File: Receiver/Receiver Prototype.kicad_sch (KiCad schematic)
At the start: 70 parts, among them J1 Conn_01x02_Socket, J10 Conn_01x01, J11 Conn_Coaxial, J12 Conn_Coaxial, J2 Conn_01x03, J3 Conn_01x01, J4 Conn_Coaxial, J5 Conn_01x01, J6 Conn_01x02, J7 Conn_Coaxial, J8 Conn_Coaxial, J9 Conn_01x01, U1 OPA3692ID, U2 AD8692ARZ, U3 OPA692IDBVR, U5 AD607ARSZ

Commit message: Receiver schematic complete. ERC not passed due to issues with GND
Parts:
- removed J2: Conn_01x03, Connector_PinHeader_2.54mm:PinHeader_1x03_P2.54mm_Vertical, symbol Connector_Generic:Conn_01x03
- removed JP1: Jumper_2_Bridged, symbol Jumper:Jumper_2_Bridged
- added C27, C33: 4.7u, Capacitor_SMD:C_0603_1608Metric_Pad1.08x0.95mm_HandSolder, symbol Device:C
- added C28, C35: 10u, Capacitor_SMD:C_0603_1608Metric_Pad1.08x0.95mm_HandSolder, symbol Device:C
- added C29, C31, C34: 0.47u, Capacitor_SMD:C_0603_1608Metric_Pad1.08x0.95mm_HandSolder, symbol Device:C
- added C30, C32, C36, C37: C, Capacitor_SMD:C_0603_1608Metric_Pad1.08x0.95mm_HandSolder, symbol Device:C
- added J13, J14: Conn_Coaxial, BNC 112404:CONN_112404_AMP, symbol Connector:Conn_Coaxial
- added J15, J16, J17, J18, J19, J2, J21, J22: Conn_01x01, Connector_PinHeader_2.54mm:PinHeader_1x01_P2.54mm_Vertical, symbol Connector_Generic:Conn_01x01
- added J23, J24: Conn_01x02, Connector_PinHeader_2.54mm:PinHeader_1x02_P2.54mm_Vertical, symbol Connector_Generic:Conn_01x02
- added R20, R22: 49.9k, Resistor_SMD:R_0603_1608Metric_Pad0.98x0.95mm_HandSolder, symbol Device:R
- added R21: 33.2k, Resistor_SMD:R_0603_1608Metric_Pad0.98x0.95mm_HandSolder, symbol Device:R
- added U4, U7: LT3045EMSE-PBF, LT3045 MSOP:MSOP12_MSE_ADI, symbol LT3045 MSOP:LT3045EMSE-PBF
- added U6: LT3094EMSE-PBF, LT3094 MSOP:05-08-1666_ADI, symbol LT3094 MSOP:LT3094EMSE-PBF
- J10, J3, J9: footprint Connector_PinSocket_2.54mm:PinSocket_1x01_P2.54mm_Vertical -> Connector_PinHeader_2.54mm:PinHeader_1x01_P2.54mm_Vertical
- J11, J12, J4, J7, J8: footprint BNC 112404:CONN_112404_AMP -> Connector_Coaxial:SMA_Amphenol_132289_EdgeMount
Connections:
- net GND: now also C27.2, C28.2, C29.2, C30.2, C31.2, C32.2, C33.2, C34.2, C35.2, J13.2 (Ext), J14.2 (Ext), R20.2, R21.2, R22.2, U4.6 (ILIM), U4.9 (GND), U4.EPAD (GND), U6.6 (ILIM), U6.9 (GND), U7.6 (ILIM), U7.9 (GND), U7.EPAD (GND)
- net IC_Gain: now also J21.1 (Pin_1)
- net IC_I: now also J23.1 (Pin_1)
- net IC_IFOP: now also J22.1 (Pin_1)
- net IC_Q: now also J23.2 (Pin_2)
- net INA: now also C36.1, C37.1
- net INB: now also C36.2, C37.2
- net Reference_In: now also J16.1 (Pin_1)
- net Reference_Out: now also J17.1 (Pin_1)
- net VCC: now also C28.1, J18.1 (Pin_1), U4.10 (OUTS), U4.11 (OUT)
- net VEE: now also C32.1, J19.1 (Pin_1), U6.10 (OUTS), U6.11 (OUT)
- net at U5.7 (GREF): now also C17.2, R16.1, U5.9 (VMID)
- net +3V renamed +3.3_out
- net +3.3_out: now also J24.2 (Pin_2)
- new net: C34.1, R21.1, U7.8 (SET)
- new net: C29.1, R22.1, U4.8 (SET)
- new net: C31.1, R20.1, U6.8 (SET)
- new net +3.3V: C35.1, J24.1 (Pin_1), U7.10 (OUTS), U7.11 (OUT)
- new net PWR+: C27.1, C33.1, J13.1 (In), J2.1 (Pin_1), U4.1 (IN), U4.4 (EN/UV), U4.7 (PGFB), U7.1 (IN), U7.4 (EN/UV), U7.7 (PGFB)
- new net PWR-: C30.1, J14.1 (In), J15.1 (Pin_1), U6.2 (IN), U6.3 (EN/UV), U6.5 (PGFB)
- no-connect marks 11 -> 24
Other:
- note added: "+3.3V circut"
- note added: "VEE circut"
- moved on the sheet: C1, C16, C17, C18, C19, C2, C20, C21, C22, C23, C24, C25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

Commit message: Receiver ready for DR2. DRC not passed due to SMA connectors
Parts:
- removed C33: 4.7u, Capacitor_SMD:C_0603_1608Metric_Pad1.08x0.95mm_HandSolder, symbol Device:C
- removed C34: 0.47u, Capacitor_SMD:C_0603_1608Metric_Pad1.08x0.95mm_HandSolder, symbol Device:C
- removed C35: 10u, Capacitor_SMD:C_0603_1608Metric_Pad1.08x0.95mm_HandSolder, symbol Device:C
- removed J16, J17, J18, J19: Conn_01x01, Connector_PinHeader_2.54mm:PinHeader_1x01_P2.54mm_Vertical, symbol Connector_Generic:Conn_01x01
- removed U7: LT3045EMSE-PBF, LT3045 MSOP:MSOP12_MSE_ADI, symbol LT3045 MSOP:LT3045EMSE-PBF
- added J17, J18, J28: Conn_01x02, Connector_PinHeader_2.54mm:PinHeader_1x02_P2.54mm_Vertical, symbol Connector_Generic:Conn_01x02
- added J20, J25: Conn_01x01, Connector_PinHeader_2.54mm:PinHeader_1x01_P2.54mm_Vertical, symbol Connector_Generic:Conn_01x01
- added J26, J27: Conn_01x03, Connector_PinHeader_2.54mm:PinHeader_1x03_P2.54mm_Vertical, symbol Connector_Generic:Conn_01x03
- C30, C32: value C -> 10u
- C31: value 0.47u -> 4.7u
- J5: footprint Connector_PinSocket_2.54mm:PinSocket_1x01_P2.54mm_Vertical -> Connector_PinHeader_2.54mm:PinHeader_1x01_P2.54mm_Vertical
- R10, R13, R14: value R -> 100
- R21: value 33.2k -> 1k
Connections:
- net +3.3V is gone; now on net VCC: J24.1 (Pin_1)
- net GND: now also D3.2 (A), D4.1 (K), R14.1, J20.1 (Pin_1), J25.1 (Pin_1); no longer R21.2
- net INA: now also J28.1 (Pin_1)
- net INB: now also J28.2 (Pin_2)
- net Inst_Out: now also J18.1 (Pin_1), J18.2 (Pin_2)
- net PWR+: now also J26.1 (Pin_1)
- net PWR-: now also U6.13 (IN), J27.1 (Pin_1); no longer U6.2 (IN)
- net Reference_Out: now also J17.1 (Pin_1), J17.2 (Pin_2)
- net VCC: now also J26.2 (Pin_2); no longer C28.1, U4.10 (OUTS), U4.11 (OUT)
- net VEE: now also J27.2 (Pin_2); no longer C32.1, U6.10 (OUTS), U6.11 (OUT)
- net at R21.1: now also U5.19 (FLTR)
- net at C22.1: now also R21.2; no longer U5.19 (FLTR)
- net +3.3_out renamed VCC_IC
- new net VCC_In: C28.1, J26.3 (Pin_3), U4.10 (OUTS), U4.11 (OUT)
- new net VEE_In: C32.1, J27.3 (Pin_3), U6.10 (OUTS), U6.11 (OUT)
- no-connect marks 24 -> 20
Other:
- note removed: "+3.3V circut"
- moved on the sheet: C19, C21, C22, C30, C31, C32, J13, J14, J15, J2, R20, U6

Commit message: DR2
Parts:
- J13, J14: footprint BNC 112404:CONN_112404_AMP -> Connector_Coaxial:BNC_Amphenol_B6252HB-NPP3G-50_Horizontal
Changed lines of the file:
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@@
 	(wire
 		(pts
-			(xy 179.07 285.75) (xy 179.07 283.21)
-		)
-		(stroke
-			(width 0)
-			(type default)
-		)
-	)
-	(wire
-		(pts
 			(xy 262.89 179.07) (xy 262.89 172.72)
 		)
@@
 			)
 		)
-		(property "Footprint" "BNC 112404:CONN_112404_AMP"
+		(property "Footprint" "Connector_Coaxial:BNC_Amphenol_B6252HB-NPP3G-50_Horizontal"
 			(at 114.3 25.4 0)
 			(effects
@@
 			)
 		)
-		(property "Footprint" "BNC 112404:CONN_112404_AMP"
+		(property "Footprint" "Connector_Coaxial:BNC_Amphenol_B6252HB-NPP3G-50_Horizontal"
 			(at 66.04 25.4 0)
 			(effects

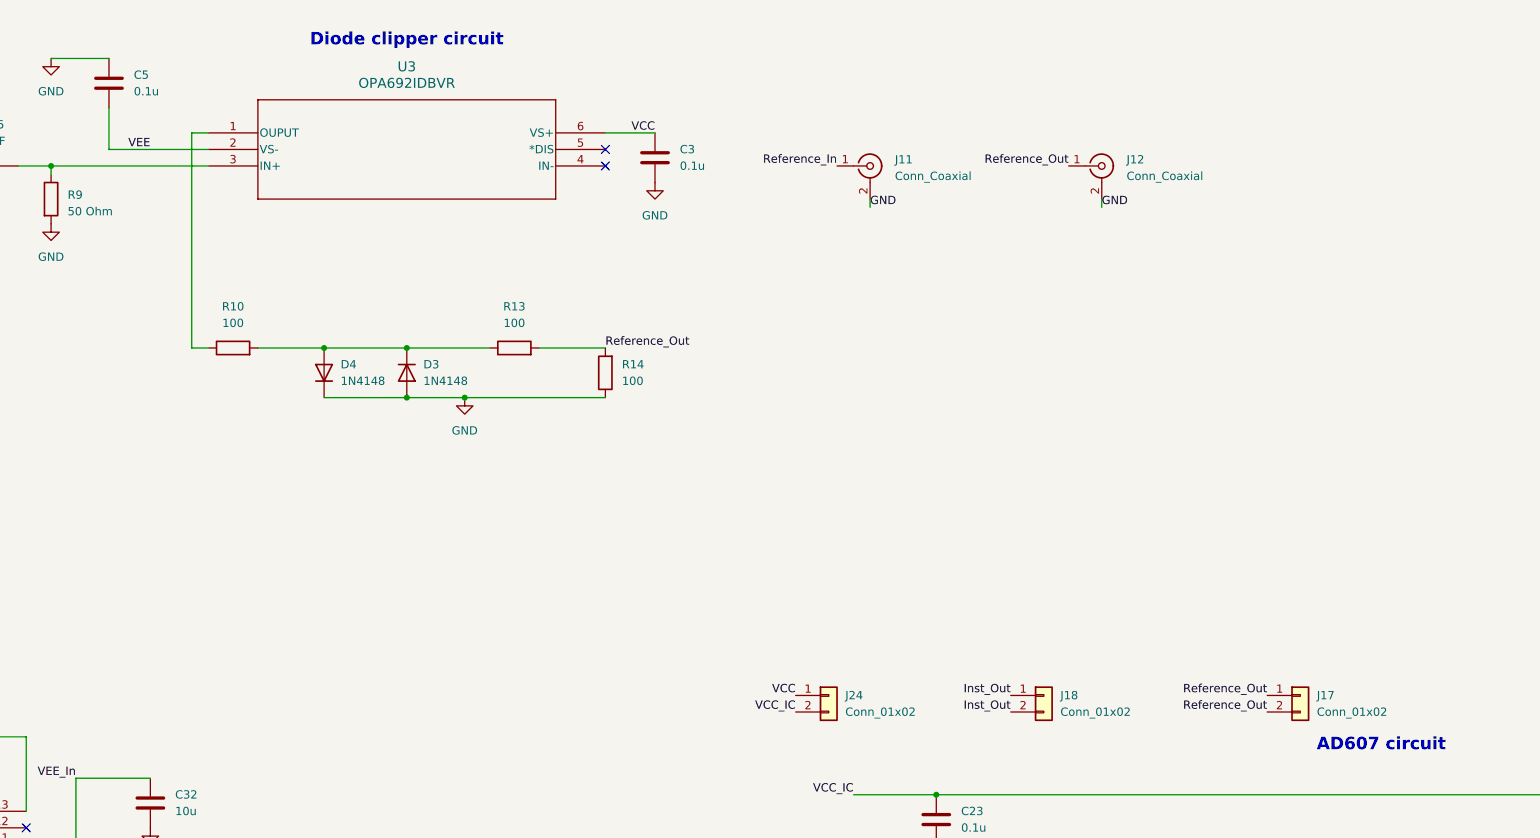
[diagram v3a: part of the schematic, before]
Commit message: Moved some components. Design not complete for the DR2
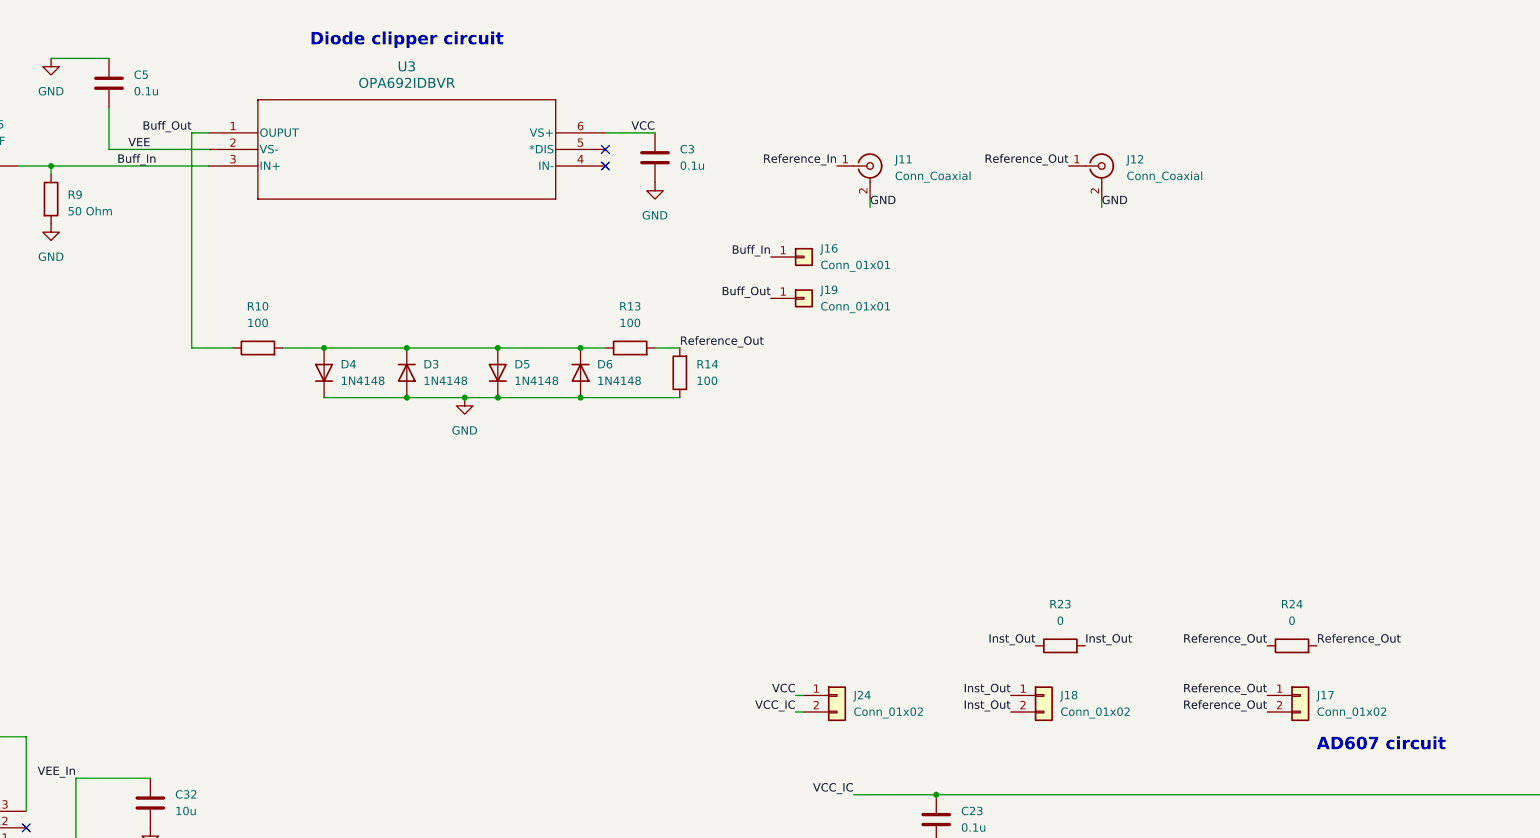
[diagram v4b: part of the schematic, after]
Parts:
- added D5, D6: 1N4148, Diode_SMD:D_0805_2012Metric_Pad1.15x1.40mm_HandSolder, symbol Diode:1N4148
- added J16, J19: Conn_01x01, Connector_PinHeader_2.54mm:PinHeader_1x01_P2.54mm_Vertical, symbol Connector_Generic:Conn_01x01
- added R23, R24: 0, Resistor_SMD:R_0603_1608Metric_Pad0.98x0.95mm_HandSolder, symbol Device:R
- J1: footprint Connector_PinSocket_2.54mm:PinSocket_1x02_P2.54mm_Vertical -> Connector_PinSocket_2.54mm:PinSocket_1x02_P2.54mm_Horizontal
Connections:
- net GND: now also D5.1 (K), D6.2 (A)
- net Inst_Out: now also R23.1, R23.2
- net Reference_Out: now also R24.1, R24.2
- net at D3.1 (K), D4.2 (A), R10.2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: now also D5.2 (A), D6.1 (K)
- net Buff_Out: now reaches R10.1, U3.1 (OUPUT)
- net Buff_Out: now also J19.1 (Pin_1)
- net Buff_In: now reaches C15.2, R9.1, U3.3 (IN+)
- net Buff_In: now also J16.1 (Pin_1)
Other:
- moved on the sheet: J24, R10, R13, R14

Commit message: Added filter input select for In-phase
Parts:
- added J29: Conn_01x03, Connector_PinHeader_2.54mm:PinHeader_1x03_P2.54mm_Vertical, symbol Connector_Generic:Conn_01x03
- added JP1: Jumper_2_Bridged, Jumper:SolderJumper-2_P1.3mm_Bridged2Bar_RoundedPad1.0x1.5mm, symbol Jumper:Jumper_2_Bridged
- added R25: 0, Resistor_SMD:R_0603_1608Metric_Pad0.98x0.95mm_HandSolder, symbol Device:R
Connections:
- net I_Filter_In: now also R24.2, J29.2 (Pin_2), R25.1; no longer J7.1 (In)
- net PWR+: now also U4.2 (IN), U4.3 (IN)
- net PWR-: now also U6.1 (IN), U6.2 (IN)
- net Reference_Out: now also JP1.1 (A), JP1.2 (B); no longer R24.1, R24.2
- net VCC_In: now also U4.12 (OUT)
- net VEE_In: now also U6.12 (OUT)
- net IC_I renamed I_Filter_In_IC
- net I_Filter_In_IC: now also J29.3 (Pin_3), R25.2
- new net I_Filter_In_Eval: J29.1 (Pin_1), J7.1 (In), R24.1
- no-connect marks 20 -> 14
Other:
- moved on the sheet: R21

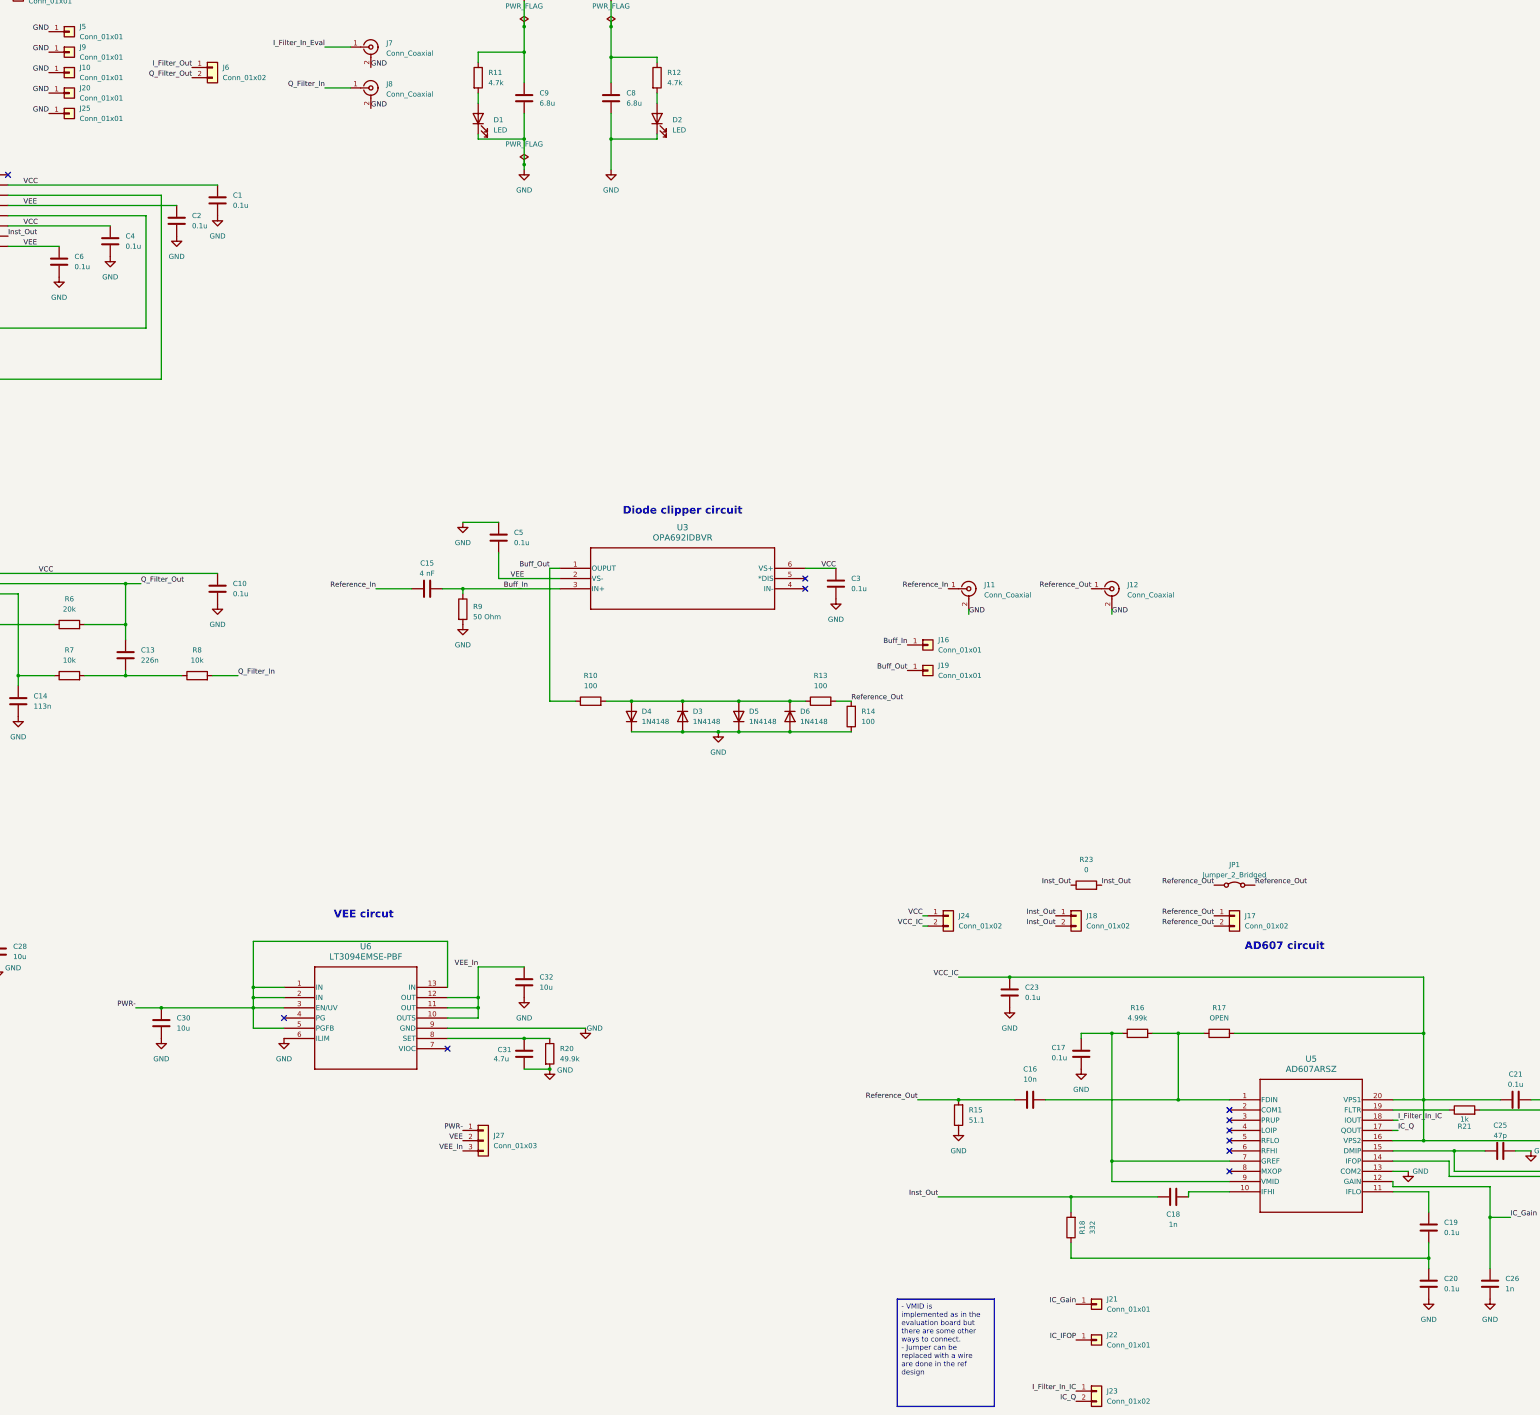
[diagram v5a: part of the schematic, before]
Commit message: Added new diodes and 3d models for BNC
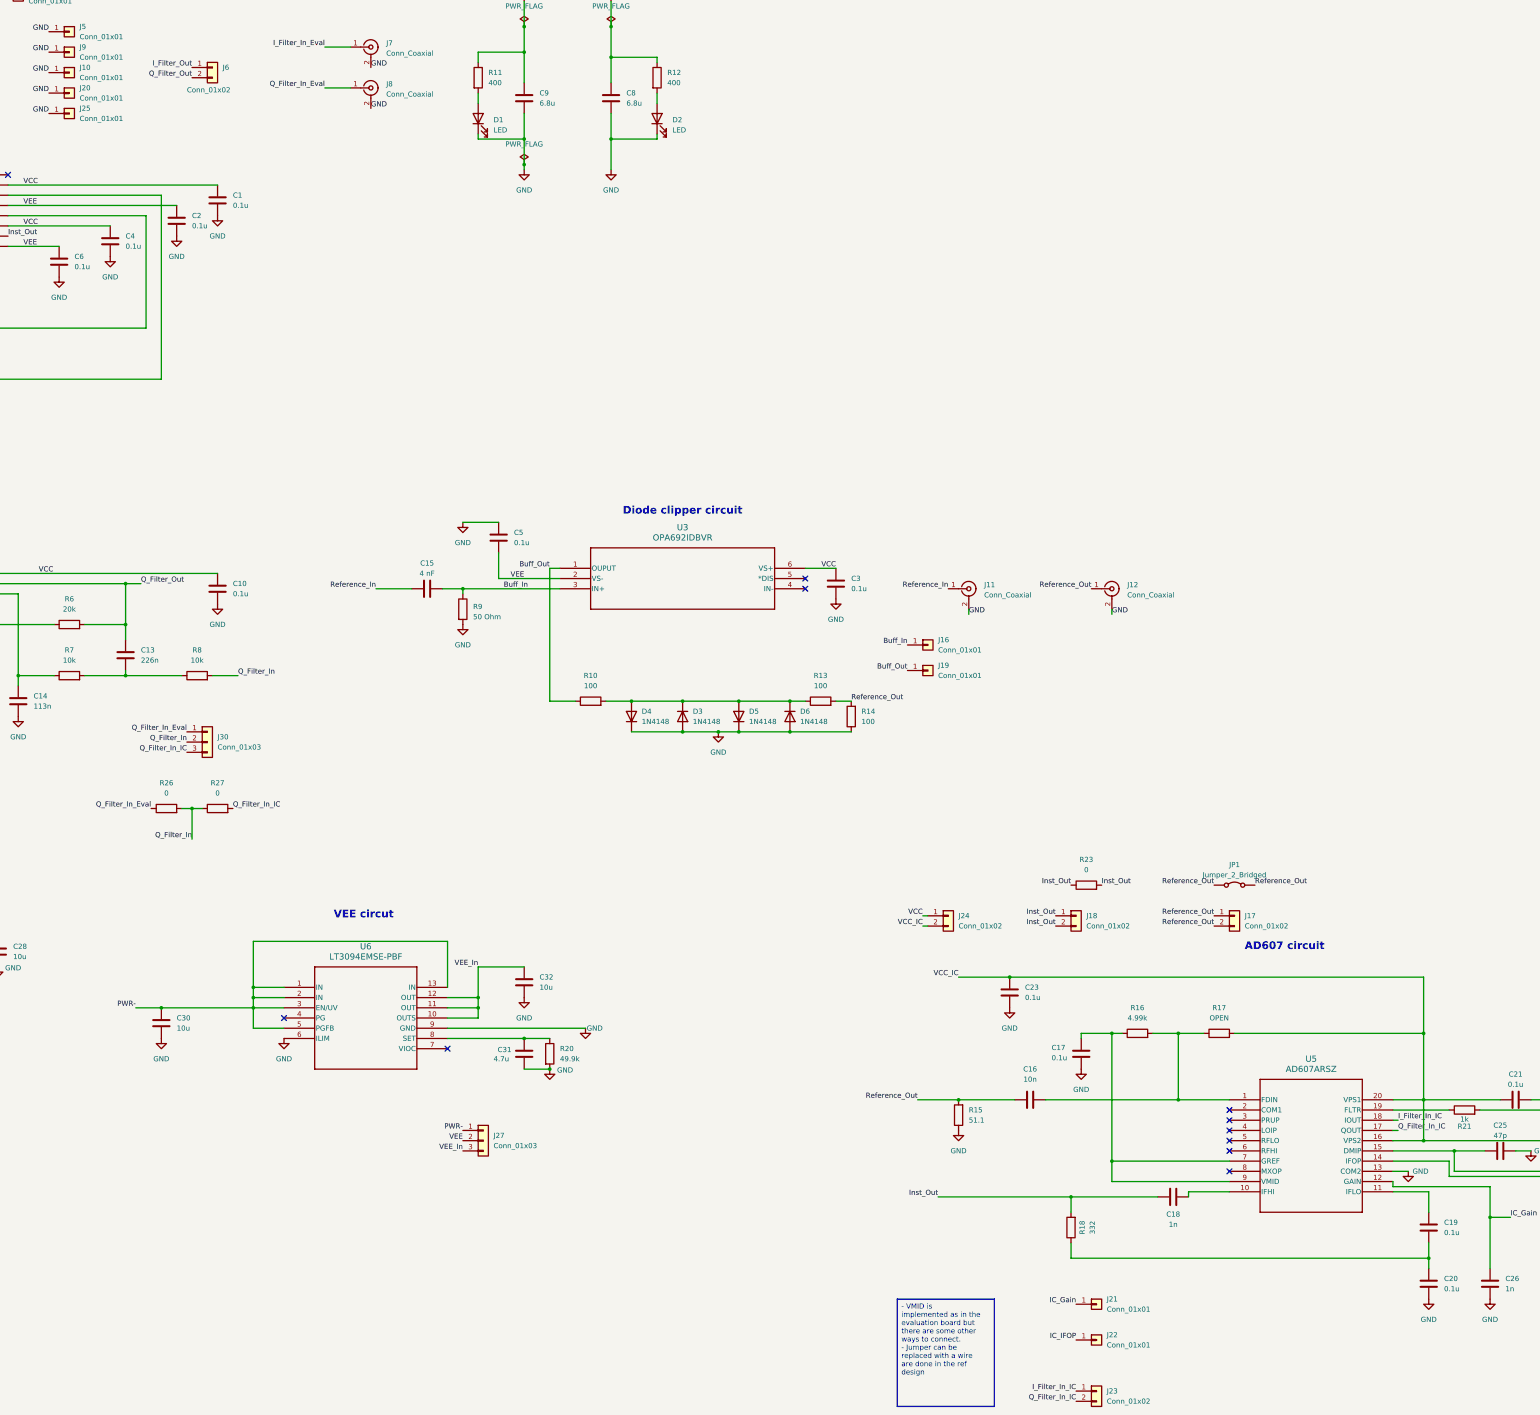
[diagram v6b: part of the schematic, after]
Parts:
- added J30: Conn_01x03, Connector_PinHeader_2.54mm:PinHeader_1x03_P2.54mm_Vertical, symbol Connector_Generic:Conn_01x03
- added R26, R27: 0, Resistor_SMD:R_0603_1608Metric_Pad0.98x0.95mm_HandSolder, symbol Device:R
- D5, D6: footprint Diode_SMD:D_0805_2012Metric_Pad1.15x1.40mm_HandSolder -> 1N4148WS-HE3-18:CR_HE3-18_VIS
- J13, J14: footprint Connector_Coaxial:BNC_Amphenol_B6252HB-NPP3G-50_Horizontal -> BNC 112640:BNC_Amphenol_112640_Edge_mount
- R11, R12: value 4.7k -> 400
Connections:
- net Q_Filter_In: now also J30.2 (Pin_2), R26.2, R27.1; no longer J8.1 (In)
- net IC_Q renamed Q_Filter_In_IC
- net Q_Filter_In_IC: now also J30.3 (Pin_3), R27.2
- new net Q_Filter_In_Eval: J30.1 (Pin_1), J8.1 (In), R26.1
